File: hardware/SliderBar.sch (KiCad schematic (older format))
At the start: 20 parts

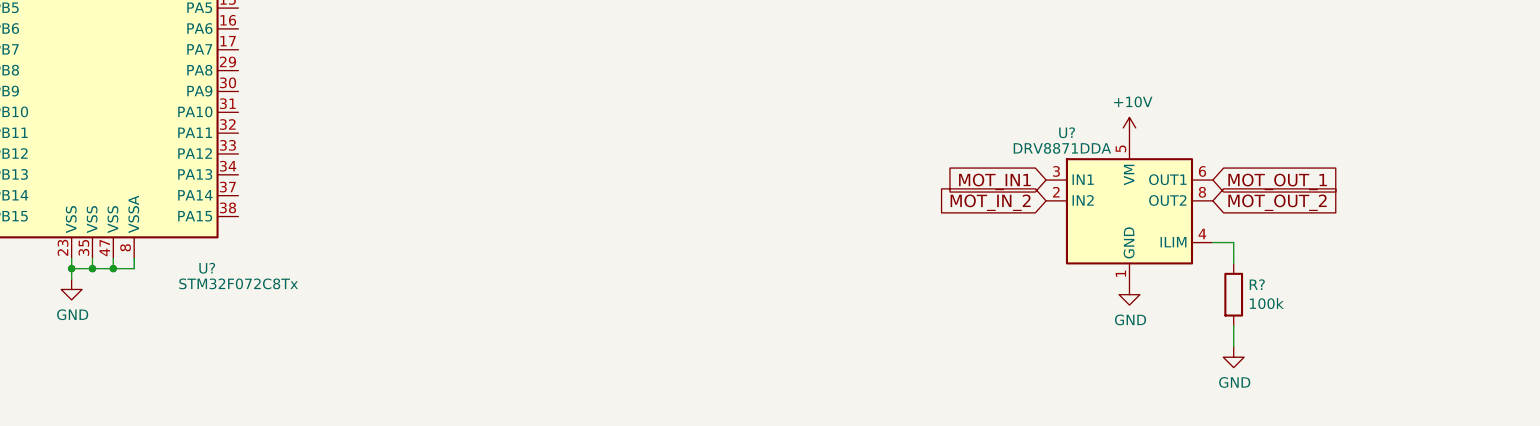
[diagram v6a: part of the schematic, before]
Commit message: Add current limits calculations
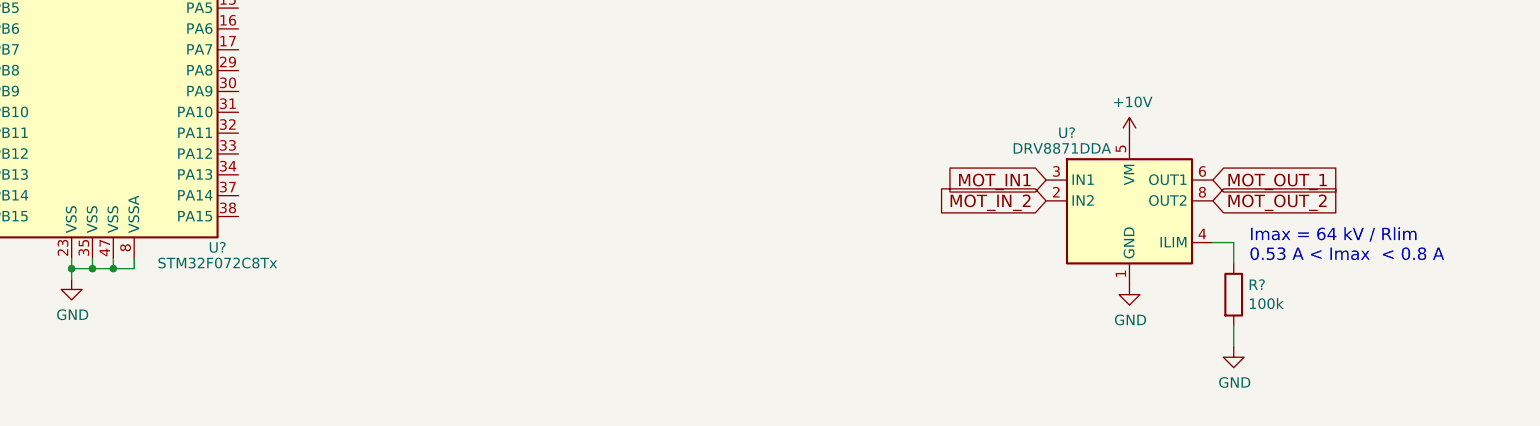
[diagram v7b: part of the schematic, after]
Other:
- note added: "Imax = 64 kV / Rlim\n0.53 A < Imax < 0.8 A"
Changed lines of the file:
@@
 U 1 1 5CFC9790
 P 8500 6175
-F 0 "U?" H 8950 4625 50  0000 C CNN
-F 1 "STM32F072C8Tx" H 9100 4550 50  0000 C CNN
+F 0 "U?" H 9000 4725 50  0000 C CNN
+F 1 "STM32F072C8Tx" H 9000 4650 50  0000 C CNN
 F 2 "Package_QFP:LQFP-48_7x7mm_P0.5mm" H 7900 4775 50  0001 R CNN
 F 3 "http://www.st.com/st-web-ui/static/active/en/resource/technical/document/datasheet/DM00090510.pdf" H 8500 6175 50  0001 C CNN
@@
 Wire Wire Line
 	13875 7600 13775 7600
+Text Notes 13950 7700 0    59   ~ 0
+Imax = 64 kV / Rlim\n0.53 A < Imax  < 0.8 A
 $EndSCHEMATC
